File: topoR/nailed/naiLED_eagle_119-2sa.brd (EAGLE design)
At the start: 12.4 x 14 mm, 9 parts, among them IC1 TCS3414

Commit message: more vias
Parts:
- C1: device dp_devices:C402 -> naiLED_eagle_119-2sa:C402
- E$1: device Logo:OSHW_FILLX100_NOTEXT -> naiLED_eagle_119-2sa:OSHW_FILLX100_NOTEXT
- IC1: device yair_r:DFN-6PIN -> naiLED_eagle_119-2sa:DFN-6PIN
- R4, R5, R6: device dp_devices:R402 -> naiLED_eagle_119-2sa:R402
- U$1: device pimoroni-optoelectronics:LED-3535 -> naiLED_eagle_119-2sa:LED-3535
- U2: device Microchip-24LCxxx:SOT95P290X145-5N -> naiLED_eagle_119-2sa:SOT95P290X145-5N
- U3: device yair_r:SOIC127P600X175-8N -> naiLED_eagle_119-2sa:SOIC127P600X175-8N
- moved IC1 0.14 mm to (9.30, 7.65)
- moved R5 0.14 mm to (6.55, 7.34)
- moved U$1 0.14 mm to (6.20, 12.0)
- moved E$1 0.14 mm to (0.81, 9.86)
- moved U3 0.14 mm to (6.10, 2.69)
- moved C1 0.14 mm to (1.68, 4.57)
- moved R6 0.14 mm to (1.68, 7.21)
- moved U2 0.14 mm to (4.32, 7.39)
- moved R4 0.14 mm to (10.5, 3.94)
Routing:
- net D3/A3: track 14.3 -> 9.86 mm, vias 0 -> 2
- net VCC: track 27.7 -> 31.1 mm, vias 0 -> 4
- net GND: track 28.7 -> 29.2 mm
- net D0/PWM/MOSI/SDA: track 20.5 -> 20.1 mm, vias 0 -> 2
- removed copper zone on layer 1, net GND
- removed copper zone on layer 16, net GND
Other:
- board text removed: "MCU"

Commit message: sent to fab, single board
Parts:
- moved E$1 0.72 mm to (0.30, 10.4)
- moved U$1 0.25 mm to (5.94, 12.0)
- moved R5 0.23 mm to (6.78, 7.39)
- moved R6 0.23 mm to (1.91, 7.24), turned to 75 degrees
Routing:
- net D4/PWM: track 12.9 -> 17.3 mm, vias 0 -> 2
- net GND: track 29.2 -> 30.5 mm, vias 0 -> 3
- net VCC: track 31.1 -> 30.0 mm
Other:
- board size 12.4 x 14 mm -> 11.6 x 14 mm

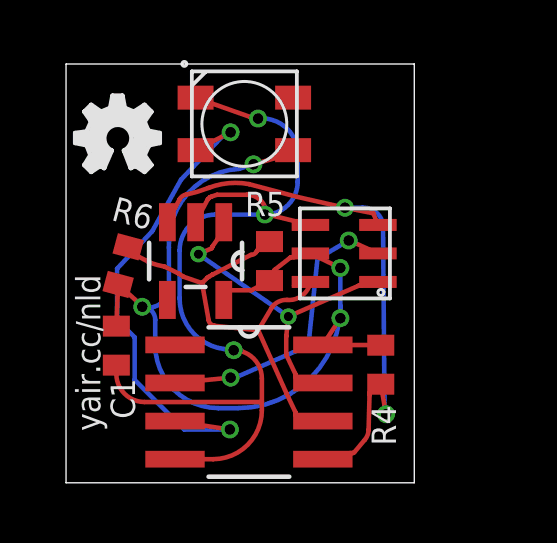
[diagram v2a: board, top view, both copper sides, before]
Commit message: ripup all, added vias to attiny
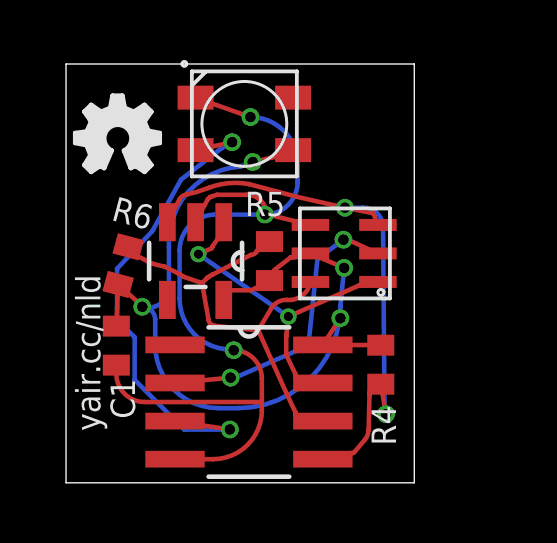
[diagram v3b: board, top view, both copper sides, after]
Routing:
- net D4/PWM: track 17.3 -> 16.7 mm
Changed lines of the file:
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@@
 <layer number="20" name="Dimension" color="15" fill="1" visible="yes" active="yes"/>
 <layer number="21" name="tPlace" color="7" fill="1" visible="yes" active="yes"/>
-<layer number="22" name="bPlace" color="7" fill="1" visible="no" active="yes"/>
+<layer number="22" name="bPlace" color="7" fill="1" visible="yes" active="yes"/>
 <layer number="23" name="tOrigins" color="15" fill="1" visible="yes" active="yes"/>
-<layer number="24" name="bOrigins" color="15" fill="1" visible="no" active="yes"/>
+<layer number="24" name="bOrigins" color="15" fill="1" visible="yes" active="yes"/>
 <layer number="25" name="tNames" color="7" fill="1" visible="yes" active="yes"/>
-<layer number="26" name="bNames" color="7" fill="1" visible="no" active="yes"/>
+<layer number="26" name="bNames" color="7" fill="1" visible="yes" active="yes"/>
 <layer number="27" name="tValues" color="7" fill="1" visible="yes" active="yes"/>
-<layer number="28" name="bValues" color="7" fill="1" visible="no" active="yes"/>
+<layer number="28" name="bValues" color="7" fill="1" visible="yes" active="yes"/>
 <layer number="29" name="tStop" color="7" fill="3" visible="no" active="yes"/>
 <layer number="30" name="bStop" color="7" fill="6" visible="no" active="yes"/>
@@
 <wire x1="8.5598" y1="4.5974" x2="9.144" y2="5.4864" width="0.1524" layer="1"/>
 <via x="9.144" y="5.4864" extent="1-16" drill="0.35"/>
-<wire x1="8.1464" y1="7.6454" x2="9.144" y2="7.1628" width="0.1524" layer="1"/>
-<via x="9.144" y="7.1628" extent="1-16" drill="0.35"/>
-<wire x1="9.144" y1="7.1628" x2="9.144" y2="5.8928" width="0.1524" layer="16"/>
+<wire x1="8.1464" y1="7.6454" x2="9.271" y2="7.1628" width="0.1524" layer="1"/>
+<via x="9.271" y="7.1628" extent="1-16" drill="0.35"/>
+<wire x1="9.271" y1="7.1628" x2="9.144" y2="5.8928" width="0.1524" layer="16"/>
 <wire x1="9.144" y1="5.8928" x2="9.144" y2="5.4864" width="0.1524" layer="16"/>
 <wire x1="1.736765625" y1="6.611146875" x2="2.5146" y2="5.9182" width="0.1524" layer="1"/>
@@
 <via x="2.54" y="5.8674" extent="1-16" drill="0.35"/>
 <wire x1="3.429" y1="7.8486" x2="3.429" y2="6.5278" width="0.1524" layer="16"/>
-<wire x1="3.429" y1="7.8486" x2="5.7658" y2="10.4648" width="0.1524" layer="16" curve="-90"/>
-<wire x1="6.2484" y1="10.6172" x2="5.7658" y2="10.4648" width="0.1524" layer="16"/>
-<via x="6.2484" y="10.6172" extent="1-16" drill="0.35"/>
-<wire x1="6.2484" y1="10.6172" x2="7.7832" y2="11.049" width="0.1524" layer="1"/>
+<wire x1="3.429" y1="7.8486" x2="5.8166" y2="10.541" width="0.1524" layer="16" curve="-90"/>
+<wire x1="6.223" y1="10.6934" x2="5.8166" y2="10.541" width="0.1524" layer="16"/>
+<via x="6.223" y="10.6934" extent="1-16" drill="0.35"/>
+<wire x1="6.223" y1="10.6934" x2="7.7832" y2="11.049" width="0.1524" layer="1"/>
 <wire x1="7.7832" y1="11.049" x2="7.5686" y2="11.0884" width="0.1524" layer="1" curve="90"/>
 <wire x1="9.144" y1="5.8928" x2="5.7404" y2="2.4892" width="0.1524" layer="16" curve="-90"/>
@@
 <wire x1="5.034584375" y1="9.6012" x2="6.031975" y2="9.6012" width="0.1524" layer="1"/>
 <wire x1="4.3186" y1="12.8384" x2="6.1468" y2="12.192" width="0.1524" layer="1"/>
-<wire x1="6.1468" y1="12.192" x2="6.4008" y2="12.1412" width="0.1524" layer="1"/>
-<via x="6.4008" y="12.1412" extent="1-16" drill="0.35"/>
-<wire x1="6.4008" y1="12.1412" x2="7.7216" y2="11.0744" width="0.1524" layer="16" curve="-90"/>
+<via x="6.1468" y="12.192" extent="1-16" drill="0.35"/>
 <wire x1="6.6294" y1="8.9408" x2="4.9784" y2="8.9408" width="0.1524" layer="16"/>
 <wire x1="4.9784" y1="8.9408" x2="3.7846" y2="7.747" width="0.1524" layer="16" curve="90"/>
@@
 <wire x1="2.6162" y1="2.6924" x2="6.4991625" y2="2.6924" width="0.1524" layer="1"/>
 <wire x1="6.4991625" y1="2.6924" x2="6.5278" y2="2.7210375" width="0.1524" layer="1" curve="90"/>
-<wire x1="7.7216" y1="11.0744" x2="7.7216" y2="10.033" width="0.1524" layer="16"/>
+<wire x1="7.7216" y1="11.0744" x2="7.7216" y2="10.414" width="0.1524" layer="16"/>
+<wire x1="7.7216" y1="10.414" x2="7.7216" y2="10.033" width="0.1524" layer="16"/>
 <wire x1="7.7216" y1="10.033" x2="6.6294" y2="8.9408" width="0.1524" layer="16" curve="-90"/>
+<wire x1="7.7216" y1="10.414" x2="7.7216" y2="10.6172" width="0.1524" layer="16"/>
+<wire x1="7.7216" y1="10.6172" x2="6.1468" y2="12.192" width="0.1524" layer="16" curve="90"/>
 </signal>
 <signal name="D4/PWM">
@@
 <wire x1="1.7018" y1="7.1374" x2="2.8702" y2="8.382" width="0.1524" layer="16"/>
 <wire x1="2.8702" y1="8.382" x2="3.8354" y2="10.1092" width="0.1524" layer="16"/>
-<wire x1="3.8354" y1="10.1092" x2="5.5372" y2="11.8872" width="0.1524" layer="16"/>
-<wire x1="5.5372" y1="11.8872" x2="5.4864" y2="11.684" width="0.1524" layer="16"/>
-<via x="5.4864" y="11.684" extent="1-16" drill="0.35"/>
-<wire x1="5.4864" y1="11.684" x2="4.3186" y2="11.0884" width="0.1524" layer="1"/>
+<wire x1="3.8354" y1="10.1092" x2="5.1816" y2="11.1506" width="0.1524" layer="16"/>
+<wire x1="5.1816" y1="11.1506" x2="5.5372" y2="11.3538" width="0.1524" layer="16"/>
+<via x="5.5372" y="11.3538" extent="1-16" drill="0.35"/>
+<wire x1="5.5372" y1="11.3538" x2="4.3186" y2="11.0884" width="0.1524" layer="1"/>
 </signal>
 <signal name="D1/PWM/MISO">
@@
 <contactref element="IC1" pad="P$2"/>
 <wire x1="10.3964" y1="7.6454" x2="9.4488" y2="8.0772" width="0.1524" layer="1"/>
-<wire x1="9.4488" y1="8.0772" x2="9.4234" y2="8.0772" width="0.1524" layer="1"/>
-<via x="9.4234" y="8.0772" extent="1-16" drill="0.35"/>
-<wire x1="9.4234" y1="8.0772" x2="8.382" y2="7.4676" width="0.1524" layer="16"/>
+<wire x1="9.4488" y1="8.0772" x2="9.2456" y2="8.1026" width="0.1524" layer="1"/>
+<via x="9.2456" y="8.1026" extent="1-16" drill="0.35"/>
+<wire x1="9.2456" y1="8.1026" x2="8.382" y2="7.4676" width="0.1524" layer="16"/>
 <wire x1="8.382" y1="7.4676" x2="8.0772" y2="4.572" width="0.1524" layer="16"/>
 <wire x1="8.0772" y1="4.572" x2="5.6388" y2="3.5052" width="0.1524" layer="16"/>
